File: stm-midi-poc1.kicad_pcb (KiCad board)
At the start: 4 copper layers, 100 x 100 mm, 117 parts, among them CN1 MIDI Out 1, CN2 MIDI In 1, CN3 MIDI Out 2, CN4 MIDI In 2, CN5 Line out, CN6 Headphone, J1 GT-USB-7010I, J2 SWD, J3 I2C, J4 UART46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

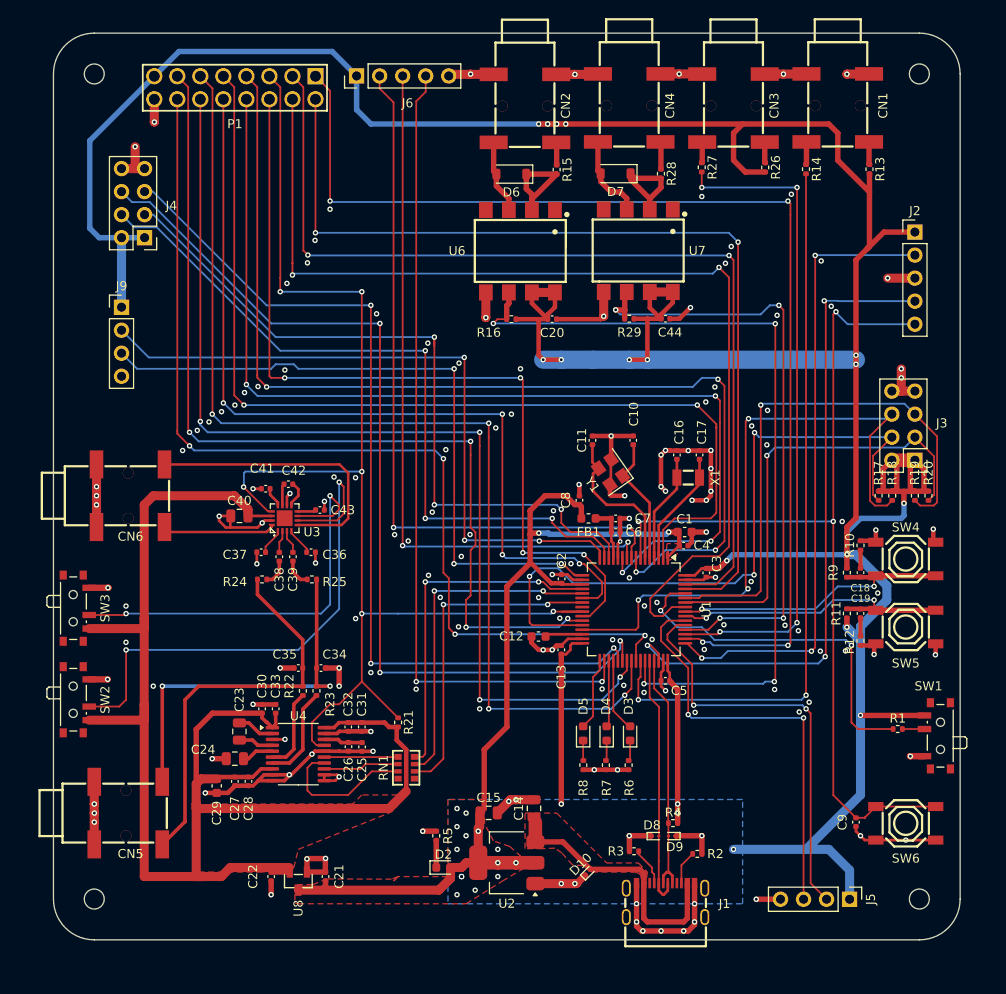
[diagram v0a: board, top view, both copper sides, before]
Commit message: All important DRC warnings addressed. Others ignored. Check against Schematic complete.
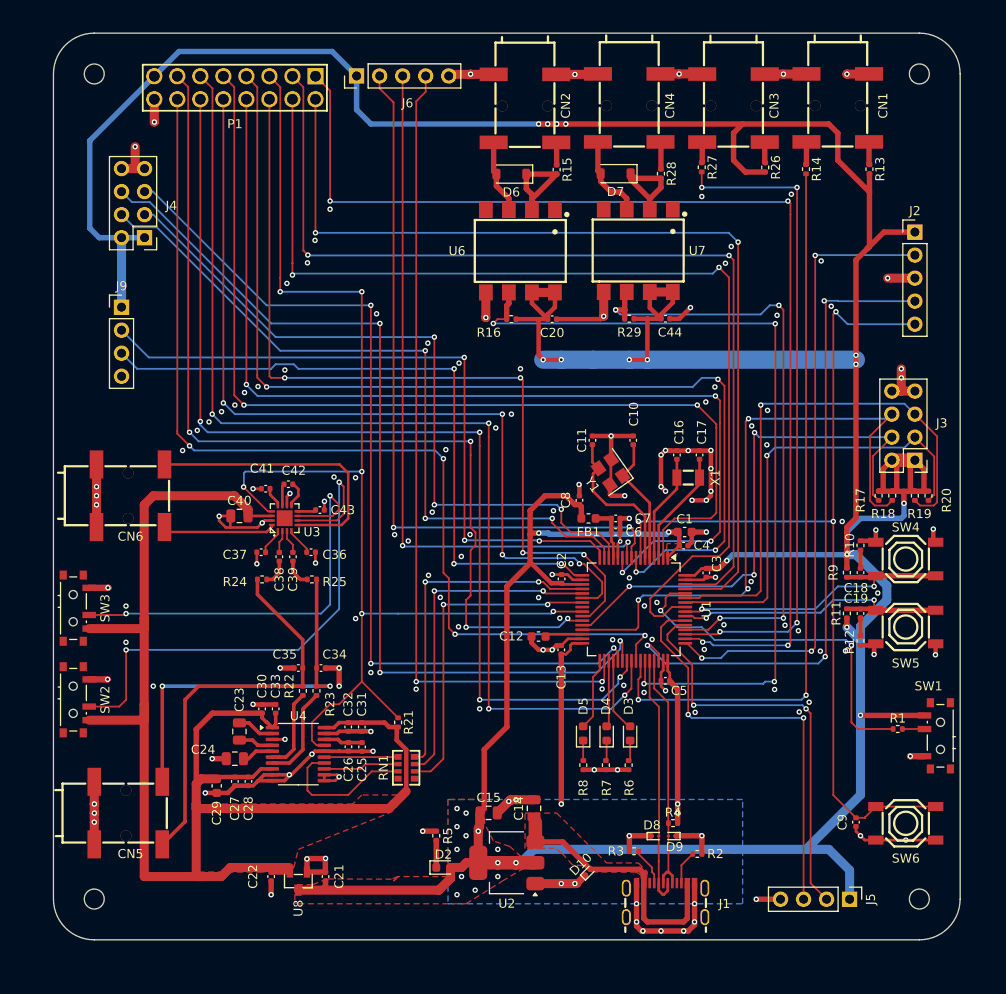
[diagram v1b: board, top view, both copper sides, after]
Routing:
- net +3V3: track 529.0 -> 555.6 mm, vias 35 -> 33
- net I2C2_SCL: track 76.4 -> 60.4 mm
- net AUDIO_MUTE: track 138.5 -> 136.1 mm
- net UART4_TX: track 80.5 -> 79.5 mm
- net GND: vias 160 -> 161
- net (no net): vias 1 -> 0

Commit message: Rotate all silkscreen up. Move all silkscreen off vias. Misc cleanups.
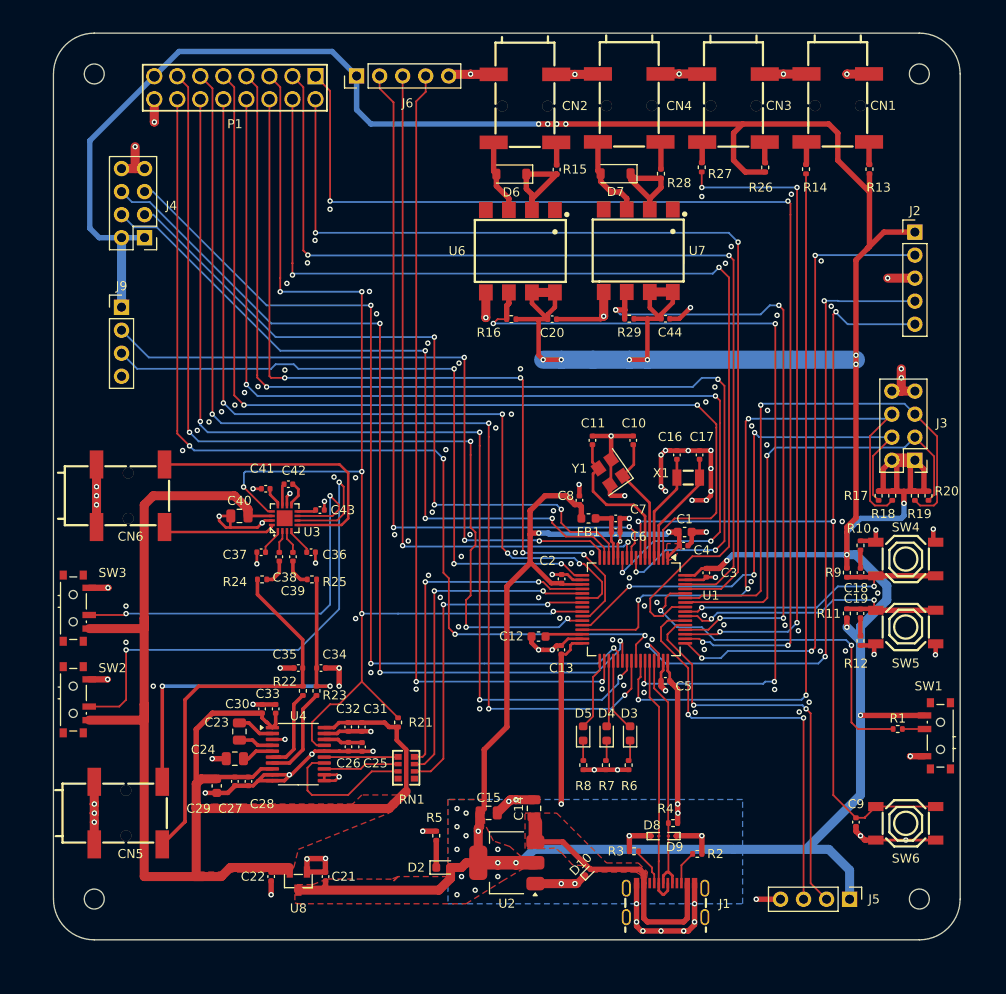
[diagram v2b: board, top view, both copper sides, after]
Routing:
- net GND: vias 161 -> 165

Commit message: More cleanups.
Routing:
- net GND: track 259.4 -> 230.3 mm, vias 165 -> 166
- net +3V3: track 555.6 -> 546.3 mm, vias 33 -> 34
- net VBUS: track 29.5 -> 27.4 mm
- net +3.3VDAC: track 168.8 -> 170.2 mm
- net GPIO_PC8: track 115.5 -> 116.3 mm
- net USART2_TX: track 75.4 -> 76.0 mm
- added copper zone on F.Cu, net GND

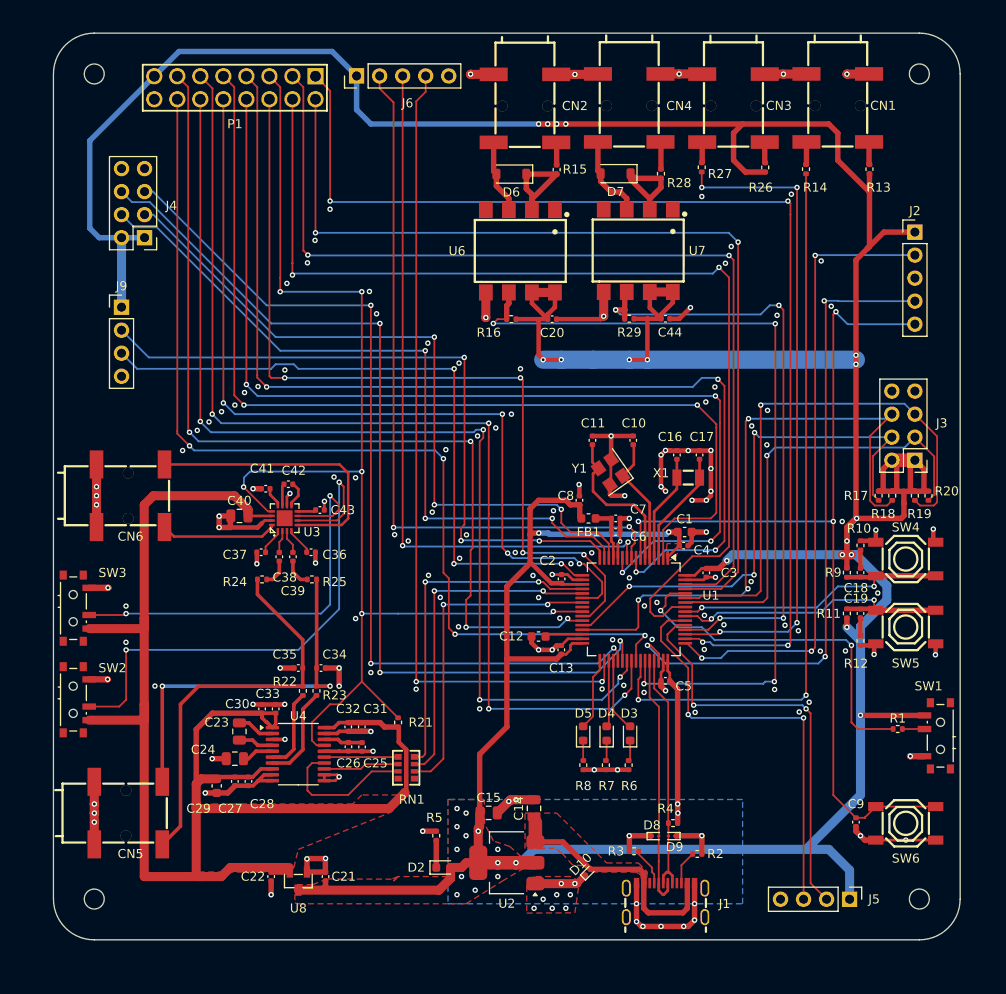
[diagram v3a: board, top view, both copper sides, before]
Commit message: Added ground fill to both signal layers, including vias where empty islands formed.
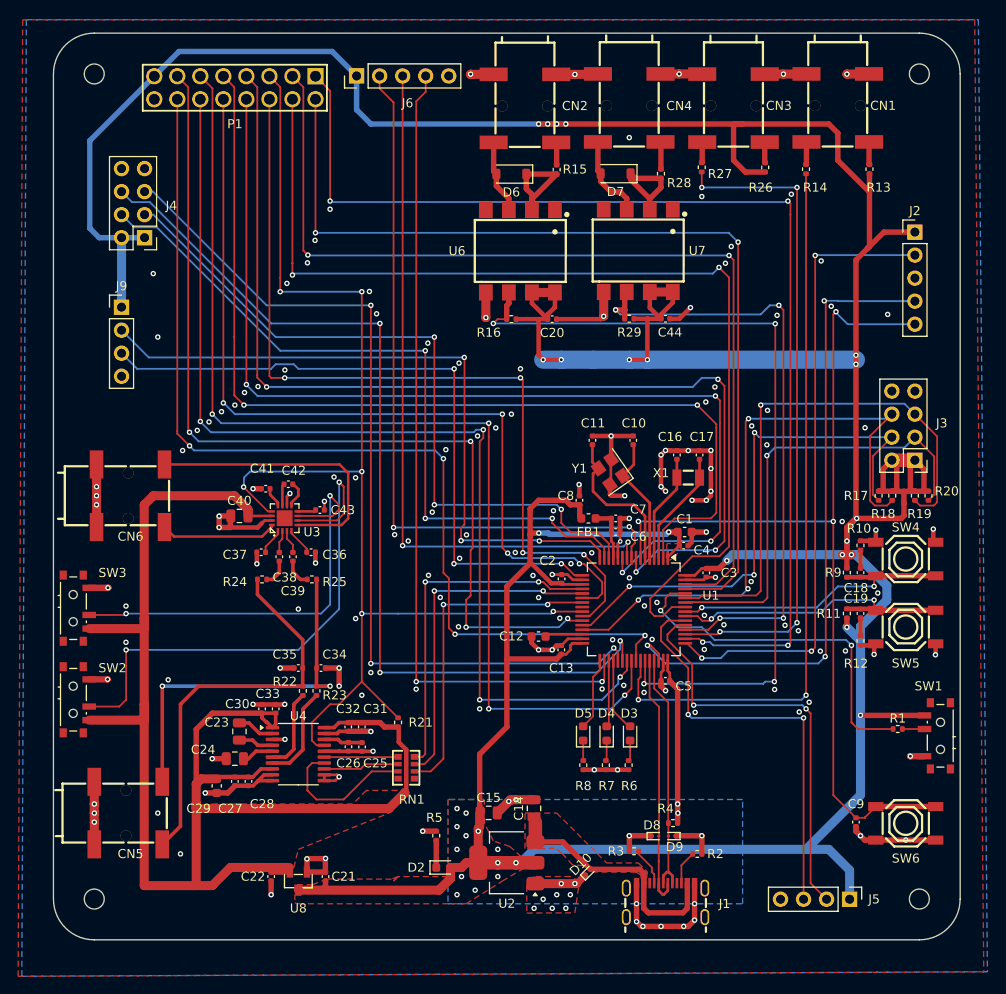
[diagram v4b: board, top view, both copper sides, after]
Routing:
- net I2C2_SDA: track 70.4 -> 68.6 mm
- net +3.3VDAC: track 170.2 -> 171.6 mm
- net +3V3: track 546.3 -> 546.9 mm
- net GND: vias 166 -> 175
- added copper zone on B.Cu, net GND

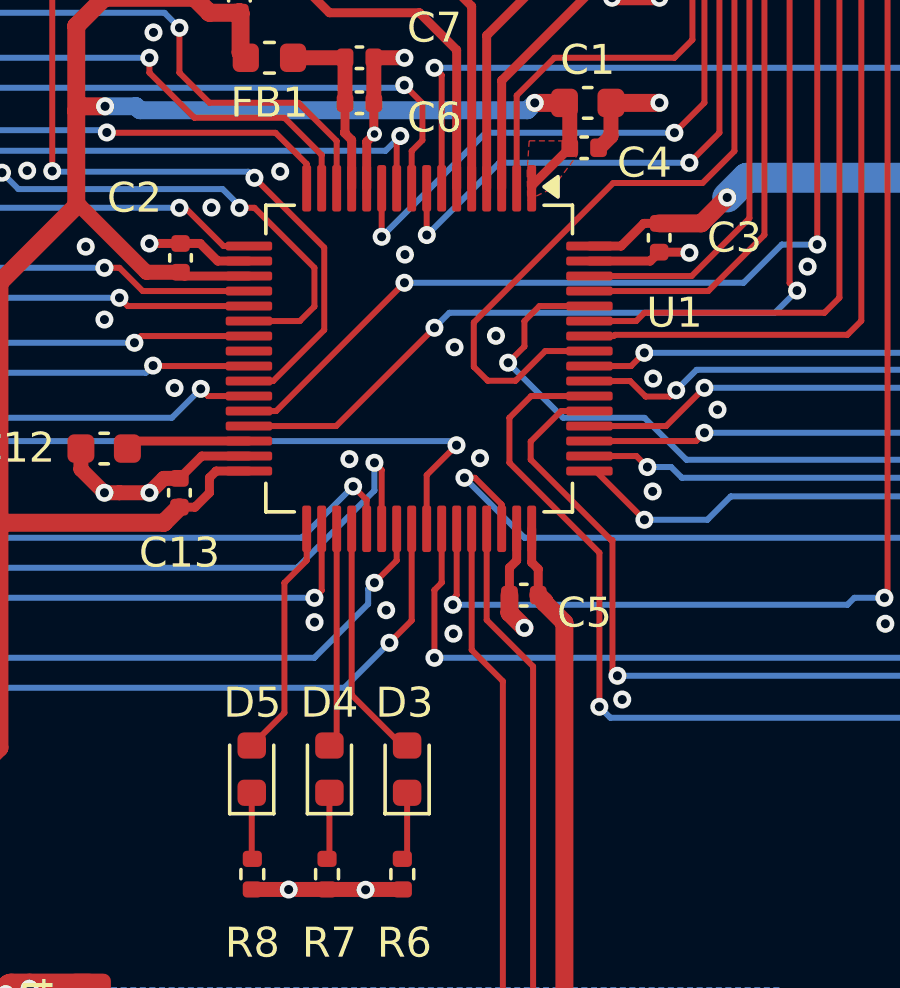
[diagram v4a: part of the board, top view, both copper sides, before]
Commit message: Added rear silk screen labels
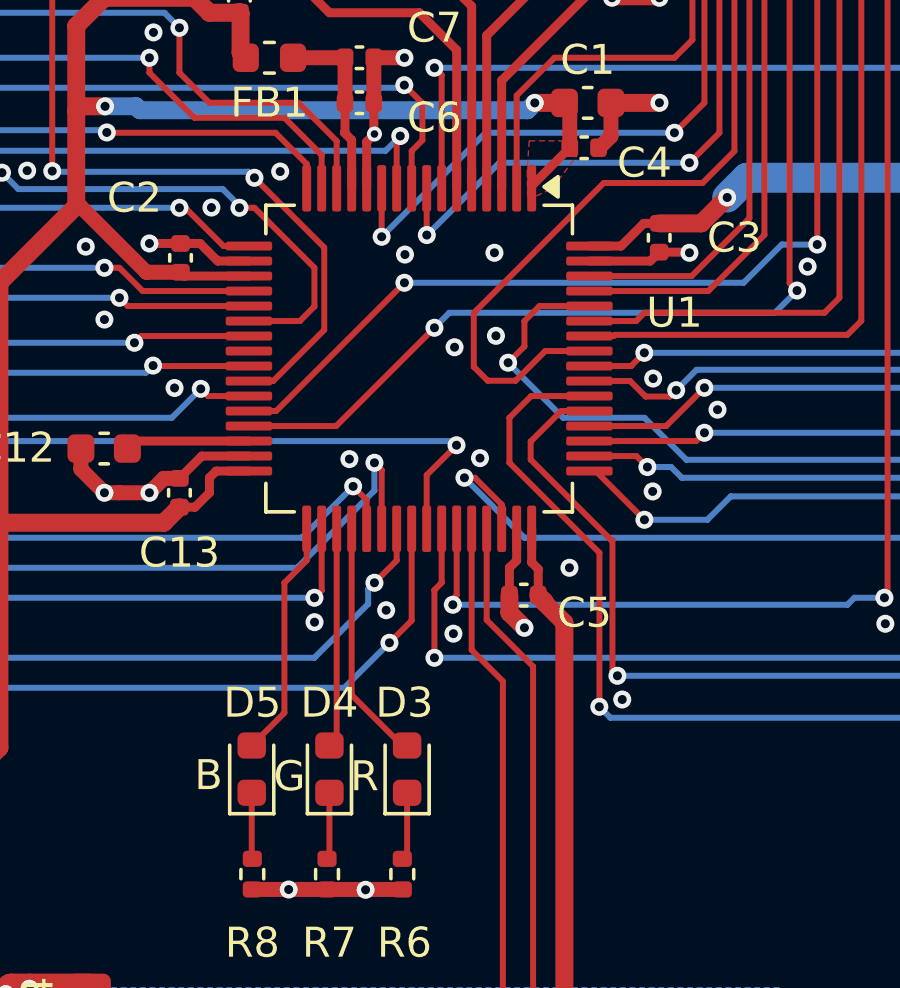
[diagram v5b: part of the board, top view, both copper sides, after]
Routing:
- net GND: vias 175 -> 177
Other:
- board text added: "1"
- board text added: "2"
- board text added: "3.3V"
- board text added: "A_M"
- board text added: "B"
- board text added: "BTN1"
- board text added: "BTN2"
- board text added: "Boot0"
- board text added: "Console (USART2)"
- board text added: "Douglas P. Fields, Jr. MIDI Synthesizer PoC1 EVT #1"
- board text added: "G"
- board text added: "GND"
- board text added: "Gain 0"
- board text added: "Gain 1"
- board text added: "Headphone Out"
- board text added: "High"
- board text added: "I2C Header"
- board text added: "Line Out"
- board text added: "Low"
- board text added: "MIDI In 1 USART 1"
- board text added: "MIDI In 2 USART 3"
- board text added: "MIDI Out 1 USART 1"
- board text added: "MIDI Out 2 USART 3"
- board text added: "MISO"
- board text added: "MOSI"
- board text added: "NRST"
- board text added: "PA15"
- board text added: "PA6"
- board text added: "PB1"
- board text added: "PB2"
- board text added: "PB5"
- board text added: "PB8"
- board text added: "PB9"
- board text added: "PC0"
- board text added: "PC3"
- board text added: "PC8"
- board text added: "PC9"
- board text added: "Power USB 2.0"
- board text added: "R"
- board text added: "RCC_MCO_1"
- board text added: "RX"
- board text added: "Reset (NRST)"
- board text added: "Rx"
- board text added: "SCK"
- board text added: "SCL"
- board text added: "SDA"
- board text added: "SPI2 Header"
- board text added: "SWCLK"
- board text added: "SWD Header"
- board text added: "SWDIO"
- board text added: "Serial"
- board text added: "TX"
- board text added: "Tx"
- board text added: "UART4"
- board text added: "UART5"
- board text added: "USART6"
- board text added: "WK4"
